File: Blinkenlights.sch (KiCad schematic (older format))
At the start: 80 parts, among them J1 PDI, U1 ATXMEGA8E5-MU

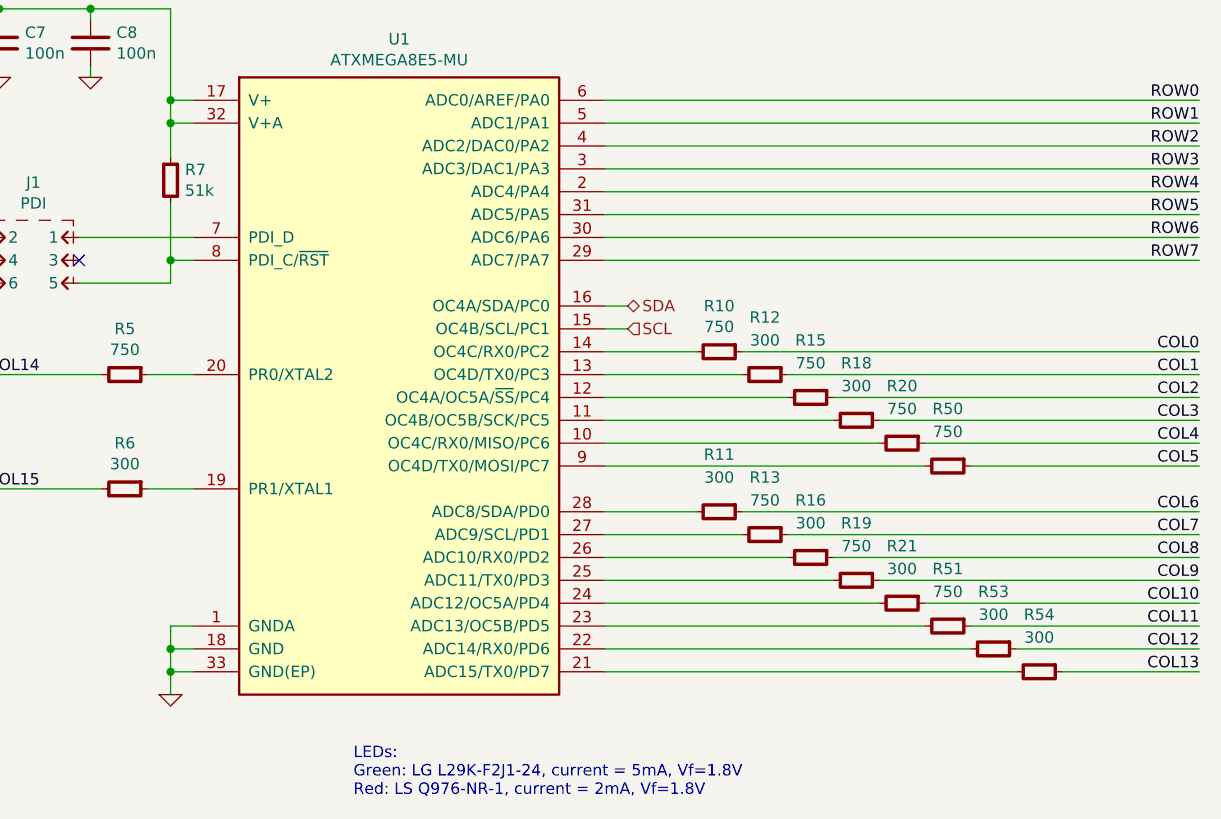
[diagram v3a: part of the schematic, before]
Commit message: Switch resistors to 0402
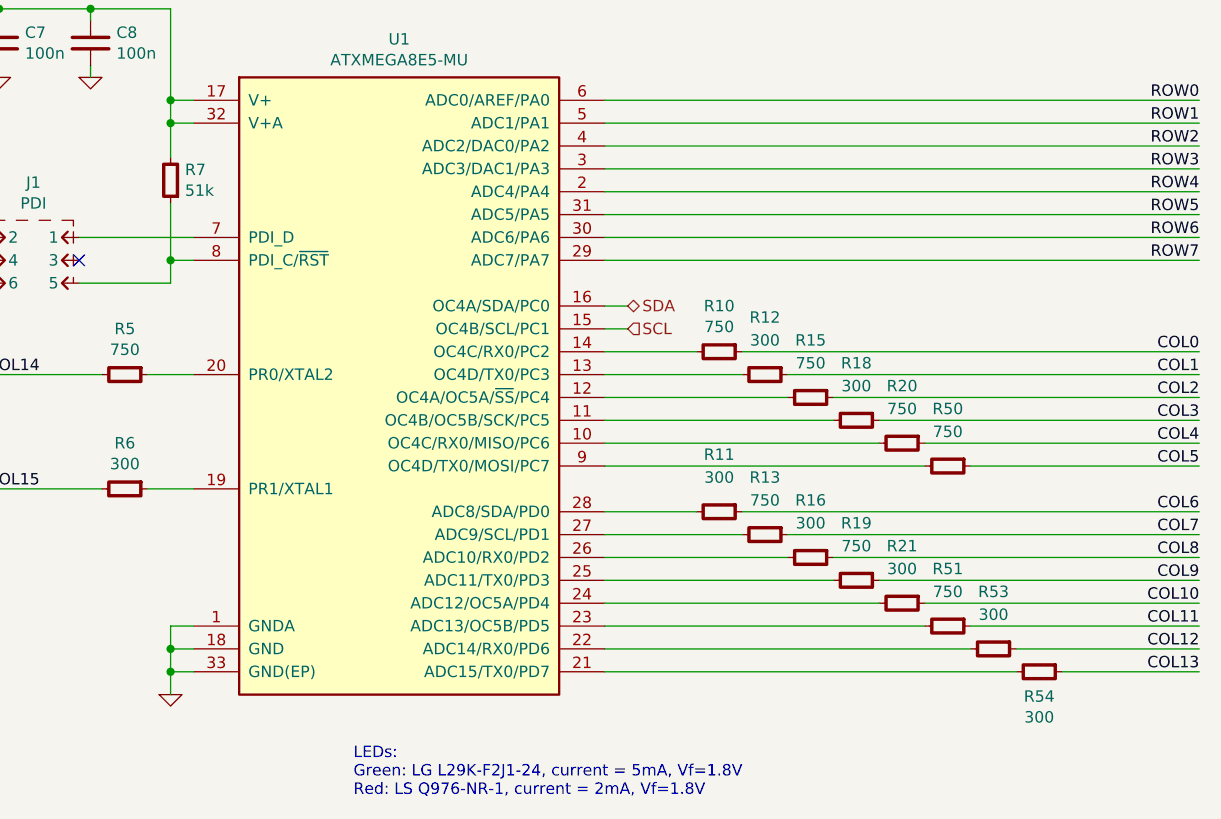
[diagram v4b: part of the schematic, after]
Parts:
- removed R10, R13, R15, R19, R20, R5, R50, R51: 750, IPC7351-Nominal:RESC1608X50, symbol R-0603
- removed R11, R12, R16, R18, R21, R53, R54, R6: 300, IPC7351-Nominal:RESC1608X50, symbol R-0603
- removed R7: 51k, IPC7351-Nominal:RESC1608X50, symbol R-0603
- added R10, R13, R15, R19, R20, R5, R50, R51: 750, IPC7351-Nominal:RESC1005X40, symbol R-0402
- added R11, R12, R16, R18, R21, R53, R54, R6: 300, IPC7351-Nominal:RESC1005X40, symbol R-0402
- added R7: 51k, IPC7351-Nominal:RESC1005X40, symbol R-0402
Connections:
- net COL0: now also R10.1
- net COL1: now also R12.1
- net COL10: now also R21.1
- net COL11: now also R51.1
- net COL12: now also R53.1
- net COL13: now also R54.1
- net COL14: now also R5.2
- net COL15: now also R6.2
- net COL2: now also R15.1
- net COL3: now also R18.1
- net COL4: now also R20.1
- net COL5: now also R50.1
- net COL6: now also R11.1
- net COL7: now also R13.1
- net COL8: now also R16.1
- net COL9: now also R19.1
- net P3V3_STBY: now also R7.2
- net at J1.5, U1.8 (PDI_C/~RST): now also R7.1
- net at U1.10 (OC4C/RX0/MISO/PC6): now also R20.2
- net at U1.11 (OC4B/OC5B/SCK/PC5): now also R18.2
- net at U1.12 (OC4A/OC5A/~SS~/PC4): now also R15.2
- net at U1.13 (OC4D/TX0/PC3): now also R12.2
- net at U1.14 (OC4C/RX0/PC2): now also R10.2
- net at U1.19 (PR1/XTAL1): now also R6.1
- net at U1.20 (PR0/XTAL2): now also R5.1
- net at U1.21 (ADC15/TX0/PD7): now also R54.2
- net at U1.22 (ADC14/RX0/PD6): now also R53.2
- net at U1.23 (ADC13/OC5B/PD5): now also R51.2
- net at U1.24 (ADC12/OC5A/PD4): now also R21.2
- net at U1.25 (ADC11/TX0/PD3): now also R19.2
- net at U1.26 (ADC10/RX0/PD2): now also R16.2
- net at U1.27 (ADC9/SCL/PD1): now also R13.2
- net at U1.28 (ADC8/SDA/PD0): now also R11.2
- net at U1.9 (OC4D/TX0/MOSI/PC7): now also R50.2

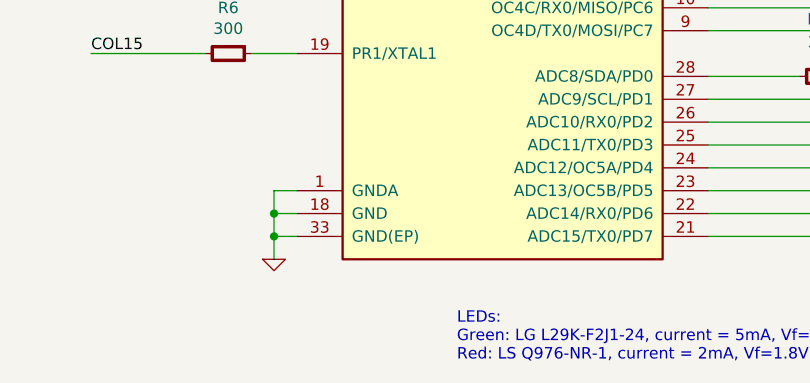
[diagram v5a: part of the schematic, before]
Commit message: Gather and assign all I2C addresses
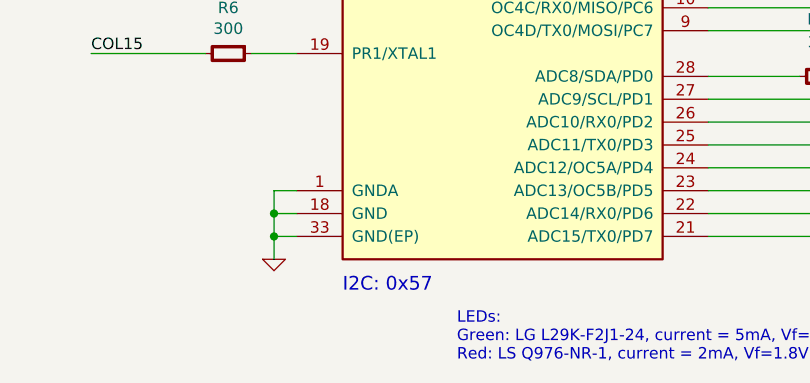
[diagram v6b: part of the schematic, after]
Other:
- note added: "I2C: 0x57"
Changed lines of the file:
@@
 	-1   0    0    1
 $EndComp
+Text Notes 2600 9650 0    60   ~ 0
+I2C: 0x57
 $EndSCHEMATC
